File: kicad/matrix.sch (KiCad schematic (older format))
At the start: 20 parts, among them J1 Conn_01x08, U1 TLC59025, U10 P-FET, U11 P-FET, U2 74HC595, U3 74HC595, U4 P-FET, U5 P-FET, U6 P-FET, U7 P-FET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

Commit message: Widen capacitor footprint pads
Easier for hand soldering.
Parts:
- C1, C2, C3: footprint Capacitor_SMD:C_0805_2012Metric_Pad1.15x1.40mm_HandSolder -> local:C_0805_2012Metric_Pad1.15x1.40mm_widepads
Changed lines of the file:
@@
 F 0 "C1" H 7140 8921 50  0000 L CNN
 F 1 "100nF" H 7140 8830 50  0000 L CNN
-F 2 "Capacitor_SMD:C_0805_2012Metric_Pad1.15x1.40mm_HandSolder" H 7063 8725 50  0001 C CNN
+F 2 "local:C_0805_2012Metric_Pad1.15x1.40mm_widepads" H 7063 8725 50  0001 C CNN
 F 3 "~" H 7025 8875 50  0001 C CNN
 	1    7025 8875
@@
 F 0 "C2" V 6698 6025 50  0000 C CNN
 F 1 "100nF" V 6789 6025 50  0000 C CNN
-F 2 "Capacitor_SMD:C_0805_2012Metric_Pad1.15x1.40mm_HandSolder" H 6988 5875 50  0001 C CNN
+F 2 "local:C_0805_2012Metric_Pad1.15x1.40mm_widepads" H 6988 5875 50  0001 C CNN
 F 3 "~" H 6950 6025 50  0001 C CNN
 	1    6950 6025
@@
 F 0 "C3" V 6573 4325 50  0000 C CNN
 F 1 "100nF" V 6664 4325 50  0000 C CNN
-F 2 "Capacitor_SMD:C_0805_2012Metric_Pad1.15x1.40mm_HandSolder" H 6863 4175 50  0001 C CNN
+F 2 "local:C_0805_2012Metric_Pad1.15x1.40mm_widepads" H 6863 4175 50  0001 C CNN
 F 3 "~" H 6825 4325 50  0001 C CNN
 	1    6825 4325

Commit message: Widen resistor pads
For easier hand soldering.
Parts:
- R1: footprint Resistor_SMD:R_1206_3216Metric_Pad1.42x1.75mm_HandSolder -> local:R_1206_3216Metric_Pad1.42x1.75mm_widepads
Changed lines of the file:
@@
 F 0 "R1" V 8693 9400 50  0000 C CNN
 F 1 "2.2K" V 8784 9400 50  0000 C CNN
-F 2 "Resistor_SMD:R_1206_3216Metric_Pad1.42x1.75mm_HandSolder" V 8830 9400 50  0001 C CNN
+F 2 "local:R_1206_3216Metric_Pad1.42x1.75mm_widepads" V 8830 9400 50  0001 C CNN
 F 3 "~" H 8900 9400 50  0001 C CNN
 	1    8900 9400

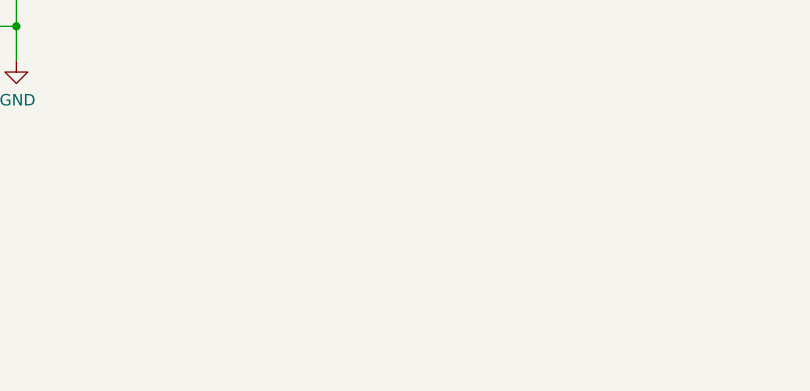
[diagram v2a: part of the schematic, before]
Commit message: Add Open Hardware and KiCad logos
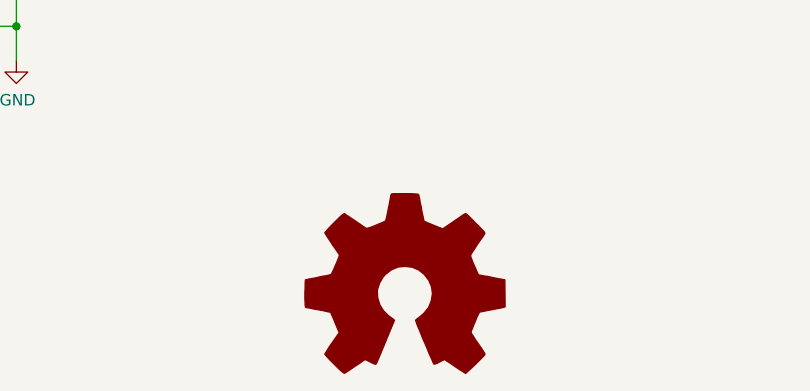
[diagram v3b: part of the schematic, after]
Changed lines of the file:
@@
 Wire Bus Line
 	10275 1525 10275 6825
+$Comp
+L Graphic:Logo_Open_Hardware_Large #LOGO1
+U 1 1 5EE98802
+P 11000 10575
+F 0 "#LOGO1" H 11000 11075 50  0001 C CNN
+F 1 "Logo_Open_Hardware_Large" H 11000 10175 50  0001 C CNN
+F 2 "" H 11000 10575 50  0001 C CNN
+F 3 "~" H 11000 10575 50  0001 C CNN
+	1    11000 10575
+	1    0    0    -1
+$EndComp
 $EndSCHEMATC

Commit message: Fix MOSFET symbol pinout
This fixes the mistake in the MOSFET symbol that incorrectly paired
up input pins 1-2 with output pins 5-6 and input 3-4 with 7-8.
Instead, pins 1-2 (source & gate) map to output pins 7-8 (drain) and
3-4 map to 5-6.

The result of this mistake in v01 of the board means that every pair
of display rows are flipped. At a high refresh rate this should not
be visible, but it does require a workaround in the driver software
that swaps the contents of every pair of display rows.
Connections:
- net ROW1: now also U4.5 (D1), U4.6 (D1); no longer U4.7 (D1), U4.8 (D1)
- net ROW13: now also U10.5 (D1), U10.6 (D1); no longer U10.7 (D1), U10.8 (D1)
- net ROW14: now also U10.7 (D1), U10.8 (D1); no longer U10.5 (D1), U10.6 (D1)
- net ROW15: now also U11.5 (D1), U11.6 (D1); no longer U11.7 (D1), U11.8 (D1)
- net ROW16: now also U11.7 (D1), U11.8 (D1); no longer U11.5 (D1), U11.6 (D1)
- net ROW2: now also U4.7 (D1), U4.8 (D1); no longer U4.5 (D1), U4.6 (D1)
- net ROW3: now also U5.5 (D1), U5.6 (D1); no longer U5.7 (D1), U5.8 (D1)
- net ROW4: now also U5.7 (D1), U5.8 (D1); no longer U5.5 (D1), U5.6 (D1)
- net ROW5: now also U6.5 (D1), U6.6 (D1); no longer U6.7 (D1), U6.8 (D1)
- net ROW6: now also U6.7 (D1), U6.8 (D1); no longer U6.5 (D1), U6.6 (D1)
- net ROW7: now also U7.5 (D1), U7.6 (D1); no longer U7.7 (D1), U7.8 (D1)
- net ROW8: now also U7.7 (D1), U7.8 (D1); no longer U7.5 (D1), U7.6 (D1)
- net at U3.4 (QE): now also U10.4 (G2); no longer U10.2 (G1)
- net at U3.5 (QF): now also U10.2 (G1); no longer U10.4 (G2)
- net at U3.6 (QG): now also U11.4 (G2); no longer U11.2 (G1)
- net at U3.7 (QH): now also U11.2 (G1); no longer U11.4 (G2)
- net at U2.1 (QB): now also U4.2 (G1); no longer U4.4 (G2)
- net at U2.15 (QA): now also U4.4 (G2); no longer U4.2 (G1)
- net at U2.2 (QC): now also U5.4 (G2); no longer U5.2 (G1)
- net at U2.3 (QD): now also U5.2 (G1); no longer U5.4 (G2)
- net at U2.4 (QE): now also U6.4 (G2); no longer U6.2 (G1)
- net at U2.5 (QF): now also U6.2 (G1); no longer U6.4 (G2)
- net at U2.6 (QG): now also U7.4 (G2); no longer U7.2 (G1)
- net at U2.7 (QH): now also U7.2 (G1); no longer U7.4 (G2)
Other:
- moved on the sheet: U10A, U10B, U11A, U11B, U4A, U4B, U5A, U5B, U6A, U6B, U7A, U7B
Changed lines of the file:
@@
 Sheet 1 1
 Title "16x16 LED Dot Matrix Display"
-Date "2020-05-31"
-Rev ""
+Date "2020-07-03"
+Rev "v0.2"
 Comp ""
 Comment1 ""
@@
 Entry Wire Line
 	10175 2225 10275 2325
-Text Label 9625 4625 0    50   ~ 0
-ROW9
 Entry Wire Line
 	10175 2625 10275 2725
@@
 L local:P-FET U4
 U 1 1 5F09B5FB
-P 9250 1425
-F 0 "U4" H 9000 1625 50  0000 C CNN
-F 1 "P-FET" V 9250 1425 50  0000 C CNN
-F 2 "local:SOIC-8_3.9x4.9mm_P1.27mm_widepads" H 9450 1825 50  0001 C CNN
-F 3 "https://www.diodes.com/assets/Datasheets/DMP3085LSD.pdf" H 9450 1825 50  0001 C CNN
-	1    9250 1425
+P 9250 1825
+F 0 "U4" H 9000 2025 50  0000 C CNN
+F 1 "P-FET" V 9250 1825 50  0000 C CNN
+F 2 "local:SOIC-8_3.9x4.9mm_P1.27mm_widepads" H 9450 2225 50  0001 C CNN
+F 3 "https://www.diodes.com/assets/Datasheets/DMP3085LSD.pdf" H 9450 2225 50  0001 C CNN
+	1    9250 1825
 	1    0    0    -1
 $EndComp
 Text Label 9625 5425 0    50   ~ 0
 ROW11
-Text Label 9625 4225 0    50   ~ 0
-ROW8
 Text Label 9625 3825 0    50   ~ 0
 ROW7
@@
 L local:P-FET U4
 U 2 1 5F127DC7
-P 9250 1825
-F 0 "U4" H 9000 2025 50  0000 C CNN
-F 1 "P-FET" V 9250 1825 50  0000 C CNN
-F 2 "local:SOIC-8_3.9x4.9mm_P1.27mm_widepads" H 9450 2225 50  0001 C CNN
-F 3 "https://www.diodes.com/assets/Datasheets/DMP3085LSD.pdf" H 9450 2225 50  0001 C CNN
-	2    9250 1825
+P 9250 1425
+F 0 "U4" H 9000 1625 50  0000 C CNN
+F 1 "P-FET" V 9250 1425 50  0000 C CNN
+F 2 "local:SOIC-8_3.9x4.9mm_P1.27mm_widepads" H 9450 1825 50  0001 C CNN
+F 3 "https://www.diodes.com/assets/Datasheets/DMP3085LSD.pdf" H 9450 1825 50  0001 C CNN
+	2    9250 1425
 	1    0    0    -1
 $EndComp
@@
 L local:P-FET U5
 U 1 1 5F137EE0
+P 9250 2625
+F 0 "U5" H 9000 2825 50  0000 C CNN
+F 1 "P-FET" V 9250 2625 50  0000 C CNN
+F 2 "local:SOIC-8_3.9x4.9mm_P1.27mm_widepads" H 9450 3025 50  0001 C CNN
+F 3 "https://www.diodes.com/assets/Datasheets/DMP3085LSD.pdf" H 9450 3025 50  0001 C CNN
+	1    9250 2625
+	1    0    0    -1
+$EndComp
+$Comp
+L local:P-FET U5
+U 2 1 5F137EEA
 P 9250 2225
 F 0 "U5" H 9000 2425 50  0000 C CNN
@@
 F 2 "local:SOIC-8_3.9x4.9mm_P1.27mm_widepads" H 9450 2625 50  0001 C CNN
 F 3 "https://www.diodes.com/assets/Datasheets/DMP3085LSD.pdf" H 9450 2625 50  0001 C CNN
-	1    9250 2225
-	1    0    0    -1
-$EndComp
-$Comp
-L local:P-FET U5
-U 2 1 5F137EEA
-P 9250 2625
-F 0 "U5" H 9000 2825 50  0000 C CNN
-F 1 "P-FET" V 9250 2625 50  0000 C CNN
-F 2 "local:SOIC-8_3.9x4.9mm_P1.27mm_widepads" H 9450 3025 50  0001 C CNN
-F 3 "https://www.diodes.com/assets/Datasheets/DMP3085LSD.pdf" H 9450 3025 50  0001 C CNN
-	2    9250 2625
+	2    9250 2225
 	1    0    0    -1
 $EndComp
@@
 L local:P-FET U6
 U 1 1 5F15A3EE
+P 9250 3425
+F 0 "U6" H 9000 3625 50  0000 C CNN
+F 1 "P-FET" V 9250 3425 50  0000 C CNN
+F 2 "local:SOIC-8_3.9x4.9mm_P1.27mm_widepads" H 9450 3825 50  0001 C CNN
+F 3 "https://www.diodes.com/assets/Datasheets/DMP3085LSD.pdf" H 9450 3825 50  0001 C CNN
+	1    9250 3425
+	1    0    0    -1
+$EndComp
+$Comp
+L local:P-FET U6
+U 2 1 5F15A3F8
 P 9250 3025
 F 0 "U6" H 9000 3225 50  0000 C CNN
@@
 F 2 "local:SOIC-8_3.9x4.9mm_P1.27mm_widepads" H 9450 3425 50  0001 C CNN
 F 3 "https://www.diodes.com/assets/Datasheets/DMP3085LSD.pdf" H 9450 3425 50  0001 C CNN
-	1    9250 3025
-	1    0    0    -1
-$EndComp
-$Comp
-L local:P-FET U6
-U 2 1 5F15A3F8
-P 9250 3425
-F 0 "U6" H 9000 3625 50  0000 C CNN
-F 1 "P-FET" V 9250 3425 50  0000 C CNN
-F 2 "local:SOIC-8_3.9x4.9mm_P1.27mm_widepads" H 9450 3825 50  0001 C CNN
-F 3 "https://www.diodes.com/assets/Datasheets/DMP3085LSD.pdf" H 9450 3825 50  0001 C CNN
-	2    9250 3425
+	2    9250 3025
 	1    0    0    -1
 $EndComp
@@
 L local:P-FET U7
 U 1 1 5F15A402
+P 9250 4225
+F 0 "U7" H 9000 4425 50  0000 C CNN
+F 1 "P-FET" V 9250 4225 50  0000 C CNN
+F 2 "local:SOIC-8_3.9x4.9mm_P1.27mm_widepads" H 9450 4625 50  0001 C CNN
+F 3 "https://www.diodes.com/assets/Datasheets/DMP3085LSD.pdf" H 9450 4625 50  0001 C CNN
+	1    9250 4225
+	1    0    0    -1
+$EndComp
+$Comp
+L local:P-FET U7
+U 2 1 5F15A40C
 P 9250 3825
 F 0 "U7" H 9000 4025 50  0000 C CNN
@@
 F 2 "local:SOIC-8_3.9x4.9mm_P1.27mm_widepads" H 9450 4225 50  0001 C CNN
 F 3 "https://www.diodes.com/assets/Datasheets/DMP3085LSD.pdf" H 9450 4225 50  0001 C CNN
-	1    9250 3825
-	1    0    0    -1
-$EndComp
-$Comp
-L local:P-FET U7
-U 2 1 5F15A40C
-P 9250 4225
-F 0 "U7" H 9000 4425 50  0000 C CNN
-F 1 "P-FET" V 9250 4225 50  0000 C CNN
-F 2 "local:SOIC-8_3.9x4.9mm_P1.27mm_widepads" H 9450 4625 50  0001 C CNN
-F 3 "https://www.diodes.com/assets/Datasheets/DMP3085LSD.pdf" H 9450 4625 50  0001 C CNN
-	2    9250 4225
+	2    9250 3825
 	1    0    0    -1
 $EndComp
@@
 L local:P-FET U10
 U 1 1 5F17DC99
+P 9250 6625
+F 0 "U10" H 9000 6825 50  0000 C CNN
+F 1 "P-FET" V 9250 6625 50  0000 C CNN
+F 2 "local:SOIC-8_3.9x4.9mm_P1.27mm_widepads" H 9450 7025 50  0001 C CNN
+F 3 "https://www.diodes.com/assets/Datasheets/DMP3085LSD.pdf" H 9450 7025 50  0001 C CNN
+	1    9250 6625
+	1    0    0    -1
+$EndComp
+$Comp
+L local:P-FET U10
+U 2 1 5F17DCA3
 P 9250 6225
 F 0 "U10" H 9000 6425 50  0000 C CNN
@@
 F 2 "local:SOIC-8_3.9x4.9mm_P1.27mm_widepads" H 9450 6625 50  0001 C CNN
 F 3 "https://www.diodes.com/assets/Datasheets/DMP3085LSD.pdf" H 9450 6625 50  0001 C CNN
-	1    9250 6225
-	1    0    0    -1
-$EndComp
-$Comp
-L local:P-FET U10
-U 2 1 5F17DCA3
-P 9250 6625
-F 0 "U10" H 9000 6825 50  0000 C CNN
-F 1 "P-FET" V 9250 6625 50  0000 C CNN
-F 2 "local:SOIC-8_3.9x4.9mm_P1.27mm_widepads" H 9450 7025 50  0001 C CNN
-F 3 "https://www.diodes.com/assets/Datasheets/DMP3085LSD.pdf" H 9450 7025 50  0001 C CNN
-	2    9250 6625
+	2    9250 6225
 	1    0    0    -1
 $EndComp
@@
 L local:P-FET U11
 U 1 1 5F17DCAD
+P 9250 7425
+F 0 "U11" H 9000 7625 50  0000 C CNN
+F 1 "P-FET" V 9250 7425 50  0000 C CNN
+F 2 "local:SOIC-8_3.9x4.9mm_P1.27mm_widepads" H 9450 7825 50  0001 C CNN
+F 3 "https://www.diodes.com/assets/Datasheets/DMP3085LSD.pdf" H 9450 7825 50  0001 C CNN
+	1    9250 7425
+	1    0    0    -1
+$EndComp
+$Comp
+L local:P-FET U11
+U 2 1 5F17DCB7
 P 9250 7025
 F 0 "U11" H 9000 7225 50  0000 C CNN
@@
 F 2 "local:SOIC-8_3.9x4.9mm_P1.27mm_widepads" H 9450 7425 50  0001 C CNN
 F 3 "https://www.diodes.com/assets/Datasheets/DMP3085LSD.pdf" H 9450 7425 50  0001 C CNN
-	1    9250 7025
-	1    0    0    -1
-$EndComp
-$Comp
-L local:P-FET U11
-U 2 1 5F17DCB7
-P 9250 7425
-F 0 "U11" H 9000 7625 50  0000 C CNN
-F 1 "P-FET" V 9250 7425 50  0000 C CNN
-F 2 "local:SOIC-8_3.9x4.9mm_P1.27mm_widepads" H 9450 7825 50  0001 C CNN
-F 3 "https://www.diodes.com/assets/Datasheets/DMP3085LSD.pdf" H 9450 7825 50  0001 C CNN
-	2    9250 7425
+	2    9250 7025
 	1    0    0    -1
 $EndComp
@@
 Wire Wire Line
 	5375 9925 5275 9925
+$Comp
+L Graphic:Logo_Open_Hardware_Large #LOGO1
+U 1 1 5EE98802
+P 11000 10575
+F 0 "#LOGO1" H 11000 11075 50  0001 C CNN
+F 1 "Logo_Open_Hardware_Large" H 11000 10175 50  0001 C CNN
+F 2 "" H 11000 10575 50  0001 C CNN
+F 3 "~" H 11000 10575 50  0001 C CNN
+	1    11000 10575
+	1    0    0    -1
+$EndComp
 Wire Bus Line
 	10275 6825 10275 9125
@@
 Wire Bus Line
 	10275 1525 10275 6825
-$Comp
-L Graphic:Logo_Open_Hardware_Large #LOGO1
-U 1 1 5EE98802
-P 11000 10575
-F 0 "#LOGO1" H 11000 11075 50  0001 C CNN
-F 1 "Logo_Open_Hardware_Large" H 11000 10175 50  0001 C CNN
-F 2 "" H 11000 10575 50  0001 C CNN
-F 3 "~" H 11000 10575 50  0001 C CNN
-	1    11000 10575
-	1    0    0    -1
-$EndComp
+Text Label 9625 4225 0    50   ~ 0
+ROW8
+Text Label 9625 4625 0    50   ~ 0
+ROW9
 $EndSCHEMATC
